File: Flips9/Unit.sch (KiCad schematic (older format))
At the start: 2 parts, among them U2 74238

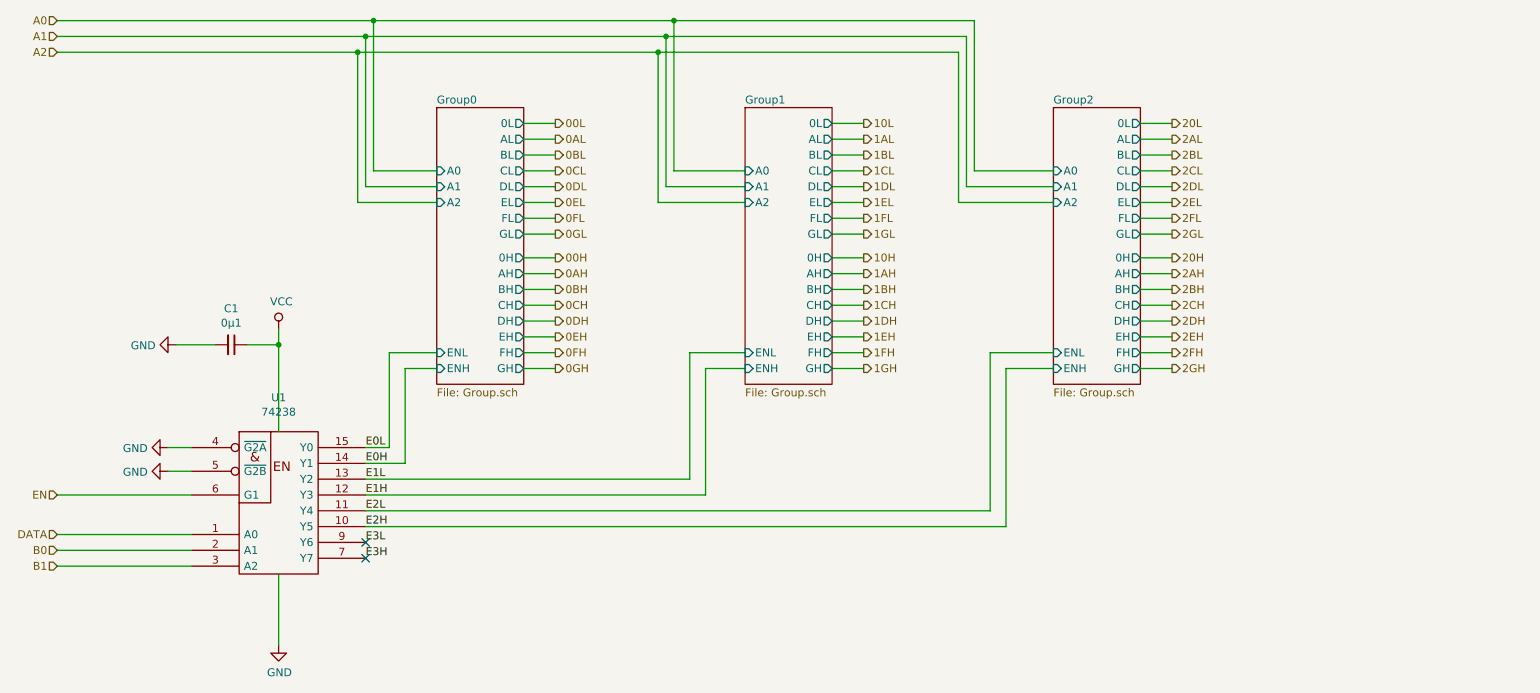
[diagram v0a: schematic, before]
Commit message: adding rows 25-32
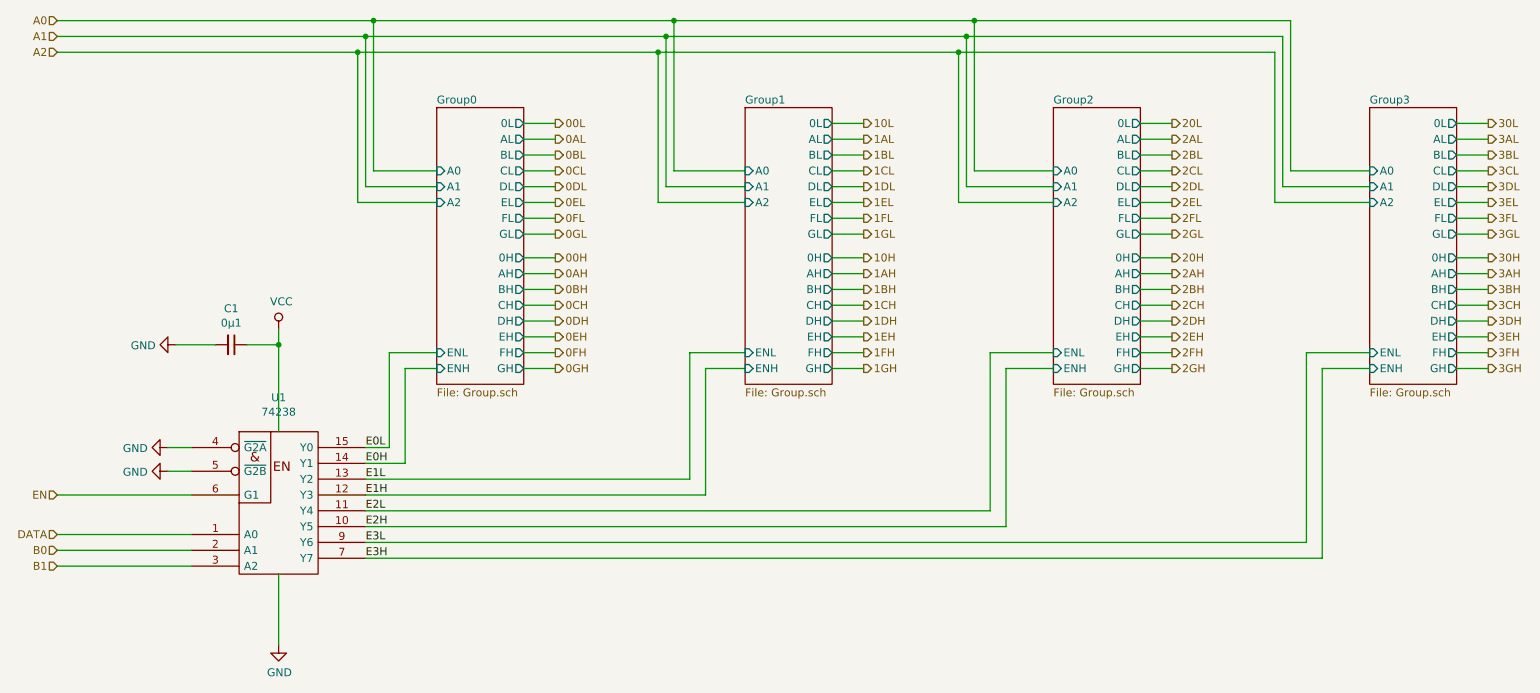
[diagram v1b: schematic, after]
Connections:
- no-connect marks 2 -> 0
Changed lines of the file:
@@
 $Descr A4 11693 8268
 encoding utf-8
-Sheet 2 5
+Sheet 2 6
 Title ""
 Date ""
@@
 Text Label 3250 5600 0    50   ~ 0
 E3H
-NoConn ~ 3250 5500
-NoConn ~ 3250 5600
+$Sheet
+S 9600 2750 550  1750
+U 5C8332F1
+F0 "Group3" 50
+F1 "Group.sch" 50
+F2 "A0" I L 9600 3150 50
+F3 "A1" I L 9600 3250 50
+F4 "A2" I L 9600 3350 50
+F5 "AL" O R 10150 2950 50
+F6 "BL" O R 10150 3050 50
+F7 "CL" O R 10150 3150 50
+F8 "DL" O R 10150 3250 50
+F9 "EL" O R 10150 3350 50
+F10 "FL" O R 10150 3450 50
+F11 "GL" O R 10150 3550 50
+F12 "AH" O R 10150 3800 50
+F13 "BH" O R 10150 3900 50
+F14 "CH" O R 10150 4000 50
+F15 "DH" O R 10150 4100 50
+F16 "EH" O R 10150 4200 50
+F17 "FH" O R 10150 4300 50
+F18 "GH" O R 10150 4400 50
+F19 "0L" O R 10150 2850 50
+F20 "0H" O R 10150 3700 50
+F21 "ENH" I L 9600 4400 50
+F22 "ENL" I L 9600 4300 50
+$EndSheet
+Wire Wire Line
+	9600 3150 9100 3150
+Wire Wire Line
+	9050 3250 9600 3250
+Wire Wire Line
+	9600 3350 9000 3350
+Wire Wire Line
+	10150 2850 10350 2850
+Wire Wire Line
+	10350 2950 10150 2950
+Wire Wire Line
+	10150 3050 10350 3050
+Wire Wire Line
+	10150 3150 10350 3150
+Wire Wire Line
+	10150 3250 10350 3250
+Wire Wire Line
+	10150 3350 10350 3350
+Wire Wire Line
+	10150 3450 10350 3450
+Wire Wire Line
+	10150 3550 10350 3550
+Wire Wire Line
+	10150 3700 10350 3700
+Wire Wire Line
+	10150 3800 10350 3800
+Wire Wire Line
+	10150 3900 10350 3900
+Wire Wire Line
+	10150 4000 10350 4000
+Wire Wire Line
+	10150 4100 10350 4100
+Wire Wire Line
+	10150 4200 10350 4200
+Wire Wire Line
+	10150 4300 10350 4300
+Wire Wire Line
+	10150 4400 10350 4400
+Wire Wire Line
+	9200 4300 9600 4300
+Wire Wire Line
+	9300 4400 9600 4400
+Text HLabel 10350 2950 2    50   Output ~ 0
+3AL
+Text HLabel 10350 3050 2    50   Output ~ 0
+3BL
+Text HLabel 10350 3150 2    50   Output ~ 0
+3CL
+Text HLabel 10350 3250 2    50   Output ~ 0
+3DL
+Text HLabel 10350 3350 2    50   Output ~ 0
+3EL
+Text HLabel 10350 3450 2    50   Output ~ 0
+3FL
+Text HLabel 10350 3550 2    50   Output ~ 0
+3GL
+Text HLabel 10350 2850 2    50   Output ~ 0
+30L
+Text HLabel 10350 3800 2    50   Output ~ 0
+3AH
+Text HLabel 10350 3900 2    50   Output ~ 0
+3BH
+Text HLabel 10350 4000 2    50   Output ~ 0
+3CH
+Text HLabel 10350 4100 2    50   Output ~ 0
+3DH
+Text HLabel 10350 4200 2    50   Output ~ 0
+3EH
+Text HLabel 10350 4300 2    50   Output ~ 0
+3FH
+Text HLabel 10350 4400 2    50   Output ~ 0
+3GH
+Text HLabel 10350 3700 2    50   Output ~ 0
+30H
+Wire Wire Line
+	3250 5500 9200 5500
+Wire Wire Line
+	9200 5500 9200 4300
+Wire Wire Line
+	9300 4400 9300 5600
+Wire Wire Line
+	9300 5600 3250 5600
+Wire Wire Line
+	7100 2200 9100 2200
+Wire Wire Line
+	9100 2200 9100 3150
+Connection ~ 7100 2200
+Wire Wire Line
+	7050 2300 9050 2300
+Wire Wire Line
+	9050 2300 9050 3250
+Connection ~ 7050 2300
+Wire Wire Line
+	7000 2400 9000 2400
+Wire Wire Line
+	9000 2400 9000 3350
+Connection ~ 7000 2400
 $EndSCHEMATC
